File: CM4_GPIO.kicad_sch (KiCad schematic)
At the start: 0 parts

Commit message: Added footprints and symbols
Could not find -on SnapEDA- MCWR06X3322FTL, MCMR06X3162FTL and USB-A-S-VT.
Power load switch NCP380HSN05AAT1G only had footprint on SnapEDA, no symbol.
Need to update HMDI footprint and symbol to correct one.
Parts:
- added C? (x2): 100n, Capacitor_SMD:C_0402_1005Metric, symbol Device:C
- added J13: 1-2199119-5, 1-2199119-5:TE_1-2199119-5, symbol 1-2199119-5:1-2199119-5
- added J?: 690-019-298-412, CM4IO:EDAC 690-019-298-412, symbol CM4IO:HDMI_A_1.4
- added Module1: ComputeModule4, CM4IO:Raspberry-Pi-4-Compute-Module, symbol CM4IO:ComputeModule4-CM4
- added U?: RT9742SNGV, Package_TO_SOT_SMD:SOT-23, symbol CM4IO:RT9742SNGV
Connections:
- new net: J13.SH1 (SHIELD), J13.SH2 (SHIELD)
- new net +5v: C?.1, U?.1 (IN)
- new net CAM0_C_N: Module1.40 (GPIO9)
- new net CAM0_C_P: Module1.42 (GND)
- new net CAM0_D0_N: Module1.28 (GPIO13)
- new net CAM0_D0_P: Module1.30 (GPIO6)
- new net CAM0_D1_N: Module1.34 (GPIO5)
- new net CAM0_D1_P: Module1.36 (ID_SD)
- new net CAM1_C_N: Module1.27 (GPIO20)
- new net CAM1_C_P: Module1.29 (GPIO16)
- new net CAM1_D0_N: Module1.15 (Ethernet_nLED3(3.3v))
- new net CAM1_D0_P: Module1.17 (Ethernet_nLED2(3.3v))
- new net CAM1_D1_N: Module1.21 (PI_nLED_Activity)
- new net CAM1_D1_P: Module1.23 (GND)
- new net CAM1_D2_N: Module1.33 (GND)
- new net CAM1_D2_P: Module1.35 (ID_SC)
- new net CAM1_D3_N: Module1.39 (GPIO8)
- new net CAM1_D3_P: Module1.41 (GPIO25)
- new net DSI0_C_N: Module1.69 (SD_DAT2)
- new net DSI0_C_P: Module1.71 (GND)
- new net DSI0_D0_N: Module1.57 (SD_CLK)
- new net DSI0_D0_P: Module1.59 (GND)
- new net DSI0_D1_N: Module1.63 (SD_DAT0)
- new net DSI0_D1_P: Module1.65 (GND)
- new net DSI1_C_N: Module1.87 (+5v_(Input))
- new net DSI1_C_P: Module1.89 (WiFi_nDisable)
- new net DSI1_D0_N: Module1.75 (SD_PWR_ON)
- new net DSI1_D0_P: Module1.77 (+5v_(Input))
- new net DSI1_D1_N: Module1.81 (+5v_(Input))
- new net DSI1_D1_P: Module1.83 (+5v_(Input))
- new net DSI1_D2_N: Module1.93 (nRPIBOOT)
- new net DSI1_D2_P: Module1.95 (nPI_LED_PWR)
- new net DSI1_D3_N: Module1.94 (AnalogIP0)
- new net DSI1_D3_P: Module1.96 (AnalogIP1)
- new net GND: C?.2, C?.2, J?.11 (CKS), J?.17 (GND), J?.2 (D2S), J?.5 (D1S), J?.8 (D0S), J?.SH1 (SH), J?.SH2 (SH), J?.SH3 (SH), J?.SH4 (SH), Module1.13 (GND), Module1.14 (GND), Module1.19 (Ethernet_nLED1(3.3v)), Module1.20 (EEPROM_nWP), Module1.25 (GPIO21), Module1.26 (GPIO19), Module1.31 (GPIO12), Module1.32 (GND), Module1.37 (GPIO7), Module1.38 (GPIO11), Module1.44 (GPIO10), Module1.50 (GPIO17), Module1.55 (GPIO14), Module1.56 (GPIO3), Module1.61 (SD_DAT3), Module1.62 (SD_CMD), Module1.67 (SD_DAT1), Module1.68 (SD_DAT4), Module1.7 (GND), Module1.73 (SD_VDD_Override), Module1.74 (GND), Module1.79 (+5v_(Input)), Module1.8 (GND), Module1.80 (SCL0), Module1.85 (+5v_(Input)), Module1.86 (+3.3v_(Output)), Module1.91 (BT_nDisable), Module1.92 (RUN_PG), Module1.97 (Camera_GPIO), Module1.98 (GND), U?.3 (GND)
- new net HDMI0_CEC: J?.13 (CEC), Module1.51 (GPIO15)
- new net HDMI0_CK_N: J?.12 (CK-), Module1.90 (+1.8v_(Output))
- new net HDMI0_CK_P: J?.10 (CK+), Module1.88 (+1.8v_(Output))
- new net HDMI0_D0_N: J?.9 (D0-), Module1.84 (+3.3v_(Output))
- new net HDMI0_D0_P: J?.7 (D0+), Module1.82 (SDA0)
- new net HDMI0_D1_N: J?.6 (D1-), Module1.78 (GPIO_VREF(1.8v/3.3v_Input))
- new net HDMI0_D1_P: J?.4 (D1+), Module1.76 (Reserved)
- new net HDMI0_D2_N: J?.3 (D2-), Module1.72 (SD_DAT6)
- new net HDMI0_D2_P: J?.1 (D2+), Module1.70 (SD_DAT7)
- new net HDMI0_HOTPLUG: J?.19 (HPD/HEAC-), Module1.53 (GND)
- new net HDMI0_SCL: J?.15 (SCL), Module1.100 (nEXTRST)
- new net HDMI0_SDA: J?.16 (SDA), Module1.99 (Global_EN)
- new net HDMI1_CEC: Module1.49 (GPIO18)
- new net HDMI1_CK_N: Module1.66 (GND)
- new net HDMI1_CK_P: Module1.64 (SD_DAT5)
- new net HDMI1_D0_N: Module1.60 (GND)
- new net HDMI1_D0_P: Module1.58 (GPIO2)
- new net HDMI1_D1_N: Module1.54 (GPIO4)
- new net HDMI1_D1_P: Module1.52 (GND)
- new net HDMI1_D2_N: Module1.48 (GPIO27)
- new net HDMI1_D2_P: Module1.46 (GPIO22)
- new net HDMI1_HOTPLUG: Module1.43 (GND)
- new net HDMI1_SCL: Module1.47 (GPIO23)
- new net HDMI1_SDA: Module1.45 (GPIO24)
- new net HDMI_5v: C?.1, J?.18 (+5V), U?.2 (OUT)
- new net PCIE_CLK_N: Module1.12 (Ethernet_Pair0_P)
- new net PCIE_CLK_P: Module1.10 (Ethernet_Pair0_N)
- new net PCIE_CLK_nREQ: Module1.2 (GND)
- new net PCIE_RX_N: Module1.18 (Ethernet_SYNC_OUT(1.8v))
- new net PCIE_RX_P: Module1.16 (Ethernet_SYNC_IN(1.8v))
- new net PCIE_TX_N: Module1.24 (GPIO26)
- new net PCIE_TX_P: Module1.22 (GND)
- new net PCIE_nRST: Module1.9 (Ethernet_Pair2_N)
- new net TV_OUT: Module1.11 (Ethernet_Pair2_P)
- new net USB2_N: Module1.3 (Ethernet_Pair3_P)
- new net USB2_P: Module1.5 (Ethernet_Pair3_N)
- new net USBOTG_ID: Module1.1 (GND)
- no-connect marks 0 -> 3
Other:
- note added: "NVME Key-M"

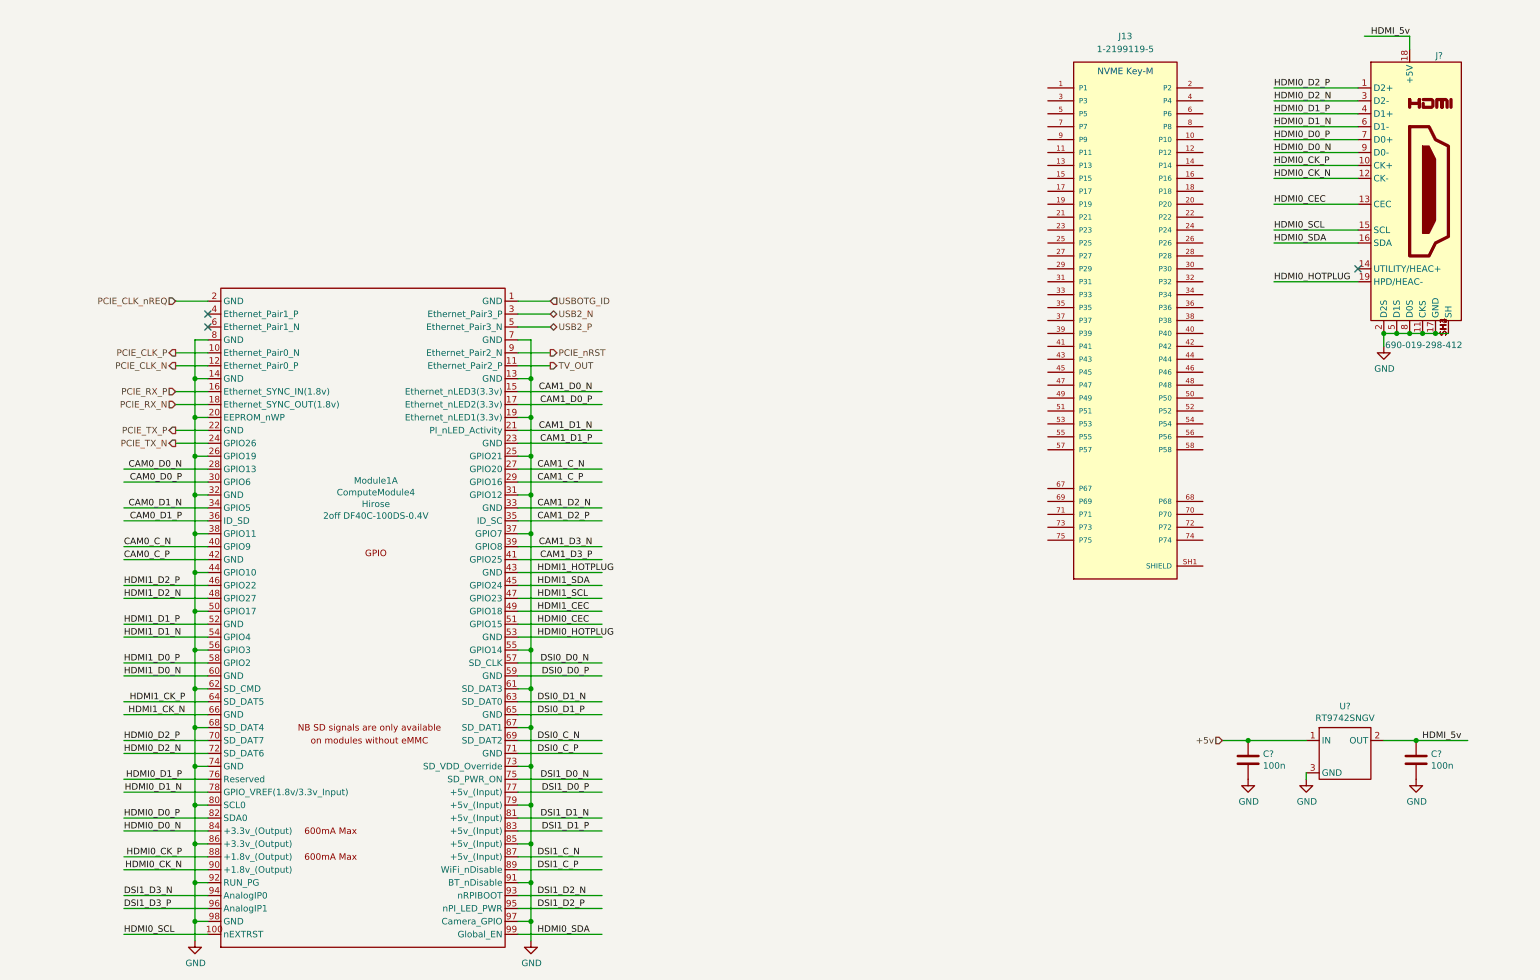
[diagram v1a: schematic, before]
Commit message: Added footprints for PCIe and added busses for PCIe and Ethernet
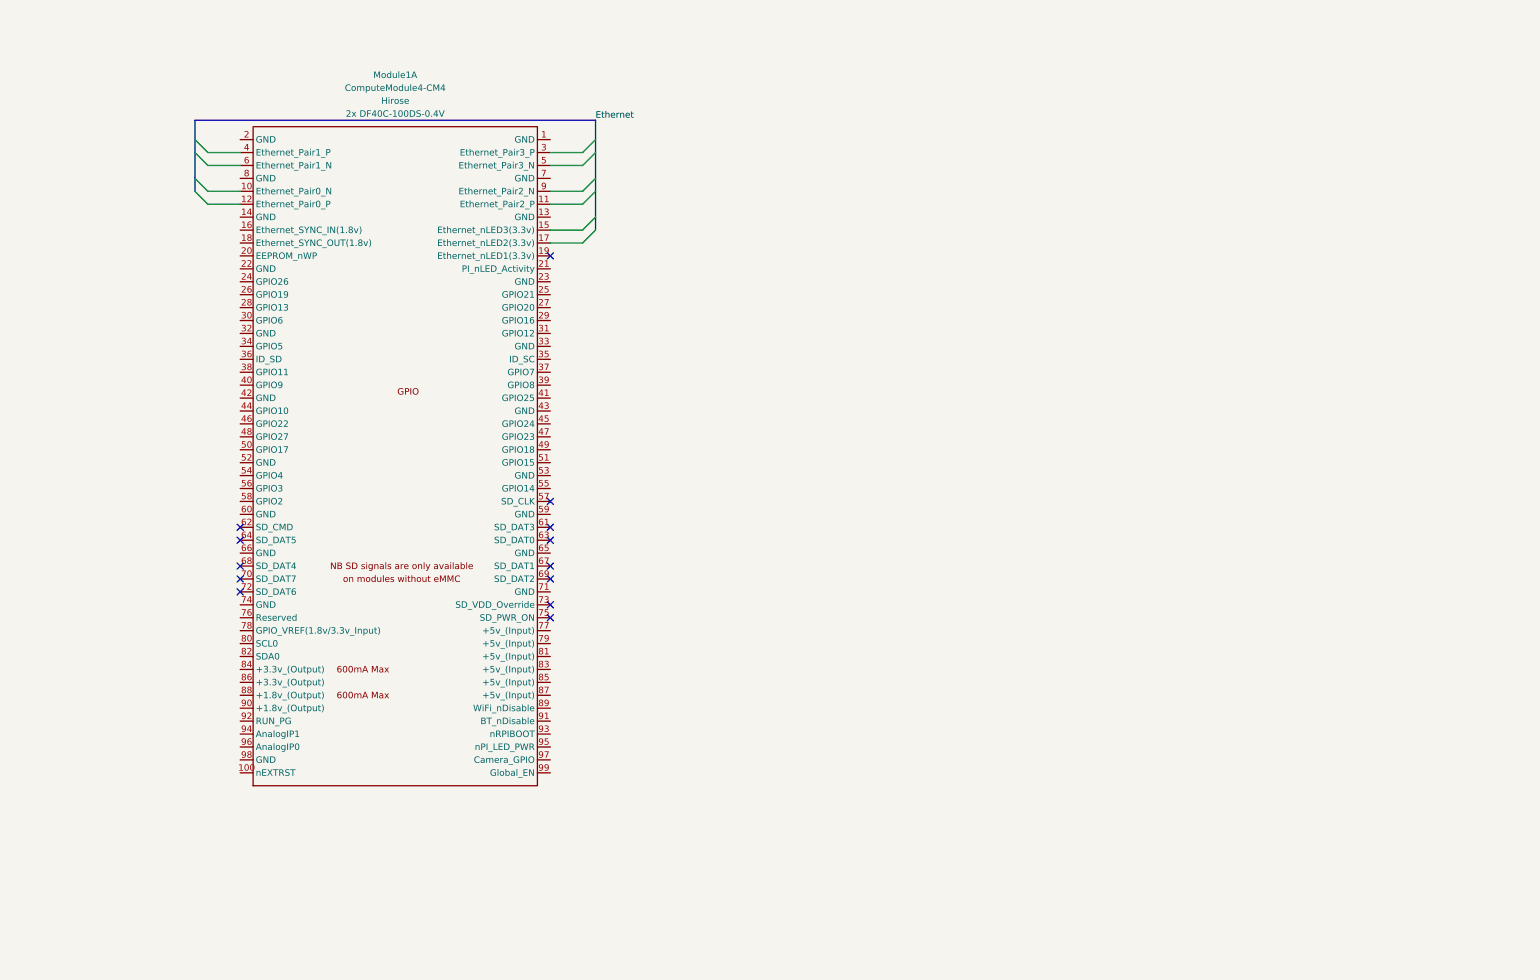
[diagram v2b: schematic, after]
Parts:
- removed C? (x2): 100n, Capacitor_SMD:C_0402_1005Metric, symbol Device:C
- removed J13: 1-2199119-5, 1-2199119-5:TE_1-2199119-5, symbol 1-2199119-5:1-2199119-5
- removed J?: 690-019-298-412, CM4IO:EDAC 690-019-298-412, symbol CM4IO:HDMI_A_1.4
- removed U?: RT9742SNGV, Package_TO_SOT_SMD:SOT-23, symbol CM4IO:RT9742SNGV
- Module1: value ComputeModule4 -> ComputeModule4-CM4; Field5 2off DF40C-100DS-0.4V -> 2x DF40C-100DS-0.4V; Field6 2off DF40C-100DS-0.4V -> (none); Field7 Hirose -> (none); Part Description 100 Position Connector Receptacle, Center Strip Contacts Su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 -> (none)
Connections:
- net CAM0_C_N: no longer names the net of Module1.40 (GPIO9)
- net CAM0_C_P: no longer names the net of Module1.42 (GND)
- net CAM0_D0_N: no longer names the net of Module1.28 (GPIO13)
- net CAM0_D0_P: no longer names the net of Module1.30 (GPIO6)
- net CAM0_D1_N: no longer names the net of Module1.34 (GPIO5)
- net CAM0_D1_P: no longer names the net of Module1.36 (ID_SD)
- net CAM1_C_N: no longer names the net of Module1.27 (GPIO20)
- net CAM1_C_P: no longer names the net of Module1.29 (GPIO16)
- net CAM1_D0_N: no longer names the net of Module1.15 (Ethernet_nLED3(3.3v))
- net CAM1_D0_P: no longer names the net of Module1.17 (Ethernet_nLED2(3.3v))
- net CAM1_D1_N: no longer names the net of Module1.21 (PI_nLED_Activity)
- net CAM1_D1_P: no longer names the net of Module1.23 (GND)
- net CAM1_D2_N: no longer names the net of Module1.33 (GND)
- net CAM1_D2_P: no longer names the net of Module1.35 (ID_SC)
- net CAM1_D3_N: no longer names the net of Module1.39 (GPIO8)
- net CAM1_D3_P: no longer names the net of Module1.41 (GPIO25)
- net DSI0_C_N: no longer names the net of Module1.69 (SD_DAT2)
- net DSI0_C_P: no longer names the net of Module1.71 (GND)
- net DSI0_D0_N: no longer names the net of Module1.57 (SD_CLK)
- net DSI0_D0_P: no longer names the net of Module1.59 (GND)
- net DSI0_D1_N: no longer names the net of Module1.63 (SD_DAT0)
- net DSI0_D1_P: no longer names the net of Module1.65 (GND)
- net DSI1_C_N: no longer names the net of Module1.87 (+5v_(Input))
- net DSI1_C_P: no longer names the net of Module1.89 (WiFi_nDisable)
- net DSI1_D0_N: no longer names the net of Module1.75 (SD_PWR_ON)
- net DSI1_D0_P: no longer names the net of Module1.77 (+5v_(Input))
- net DSI1_D1_N: no longer names the net of Module1.81 (+5v_(Input))
- net DSI1_D1_P: no longer names the net of Module1.83 (+5v_(Input))
- net DSI1_D2_N: no longer names the net of Module1.93 (nRPIBOOT)
- net DSI1_D2_P: no longer names the net of Module1.95 (nPI_LED_PWR)
- net DSI1_D3_N: no longer names the net of Module1.94 (AnalogIP1)
- net DSI1_D3_P: no longer names the net of Module1.96 (AnalogIP0)
- removed net GND: Module1.13 (GND), Module1.14 (GND), Module1.19 (Ethernet_nLED1(3.3v)), Module1.20 (EEPROM_nWP), Module1.25 (GPIO21), Module1.26 (GPIO19), Module1.31 (GPIO12), Module1.32 (GND), Module1.37 (GPIO7), Module1.38 (GPIO11), Module1.44 (GPIO10), Module1.50 (GPIO17), Module1.55 (GPIO14), Module1.56 (GPIO3), Module1.61 (SD_DAT3), Module1.62 (SD_CMD), Module1.67 (SD_DAT1), Module1.68 (SD_DAT4), Module1.7 (GND), Module1.73 (SD_VDD_Override), Module1.74 (GND), Module1.79 (+5v_(Input)), Module1.8 (GND), Module1.80 (SCL0), Module1.85 (+5v_(Input)), Module1.86 (+3.3v_(Output)), Module1.91 (BT_nDisable), Module1.92 (RUN_PG), Module1.97 (Camera_GPIO), Module1.98 (GND)
- net HDMI0_CEC: no longer names the net of Module1.51 (GPIO15)
- net HDMI0_CK_N: no longer names the net of Module1.90 (+1.8v_(Output))
- net HDMI0_CK_P: no longer names the net of Module1.88 (+1.8v_(Output))
- net HDMI0_D0_N: no longer names the net of Module1.84 (+3.3v_(Output))
- net HDMI0_D0_P: no longer names the net of Module1.82 (SDA0)
- net HDMI0_D1_N: no longer names the net of Module1.78 (GPIO_VREF(1.8v/3.3v_Input))
- net HDMI0_D1_P: no longer names the net of Module1.76 (Reserved)
- net HDMI0_D2_N: no longer names the net of Module1.72 (SD_DAT6)
- net HDMI0_D2_P: no longer names the net of Module1.70 (SD_DAT7)
- net HDMI0_HOTPLUG: no longer names the net of Module1.53 (GND)
- net HDMI0_SCL: no longer names the net of Module1.100 (nEXTRST)
- net HDMI0_SDA: no longer names the net of Module1.99 (Global_EN)
- net HDMI1_CEC: no longer names the net of Module1.49 (GPIO18)
- net HDMI1_CK_N: no longer names the net of Module1.66 (GND)
- net HDMI1_CK_P: no longer names the net of Module1.64 (SD_DAT5)
- net HDMI1_D0_N: no longer names the net of Module1.60 (GND)
- net HDMI1_D0_P: no longer names the net of Module1.58 (GPIO2)
- net HDMI1_D1_N: no longer names the net of Module1.54 (GPIO4)
- net HDMI1_D1_P: no longer names the net of Module1.52 (GND)
- net HDMI1_D2_N: no longer names the net of Module1.48 (GPIO27)
- net HDMI1_D2_P: no longer names the net of Module1.46 (GPIO22)
- net HDMI1_HOTPLUG: no longer names the net of Module1.43 (GND)
- net HDMI1_SCL: no longer names the net of Module1.47 (GPIO23)
- net HDMI1_SDA: no longer names the net of Module1.45 (GPIO24)
- net PCIE_CLK_N: no longer names the net of Module1.12 (Ethernet_Pair0_P)
- net PCIE_CLK_P: no longer names the net of Module1.10 (Ethernet_Pair0_N)
- net PCIE_CLK_nREQ: no longer names the net of Module1.2 (GND)
- net PCIE_RX_N: no longer names the net of Module1.18 (Ethernet_SYNC_OUT(1.8v))
- net PCIE_RX_P: no longer names the net of Module1.16 (Ethernet_SYNC_IN(1.8v))
- net PCIE_TX_N: no longer names the net of Module1.24 (GPIO26)
- net PCIE_TX_P: no longer names the net of Module1.22 (GND)
- net PCIE_nRST: no longer names the net of Module1.9 (Ethernet_Pair2_N)
- net TV_OUT: no longer names the net of Module1.11 (Ethernet_Pair2_P)
- net USB2_N: no longer names the net of Module1.3 (Ethernet_Pair3_P)
- net USB2_P: no longer names the net of Module1.5 (Ethernet_Pair3_N)
- net USBOTG_ID: no longer names the net of Module1.1 (GND)
- no-connect marks 3 -> 13
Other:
- note removed: "NVME Key-M"

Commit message: Cleaned up schematics and added gnds and no-connects
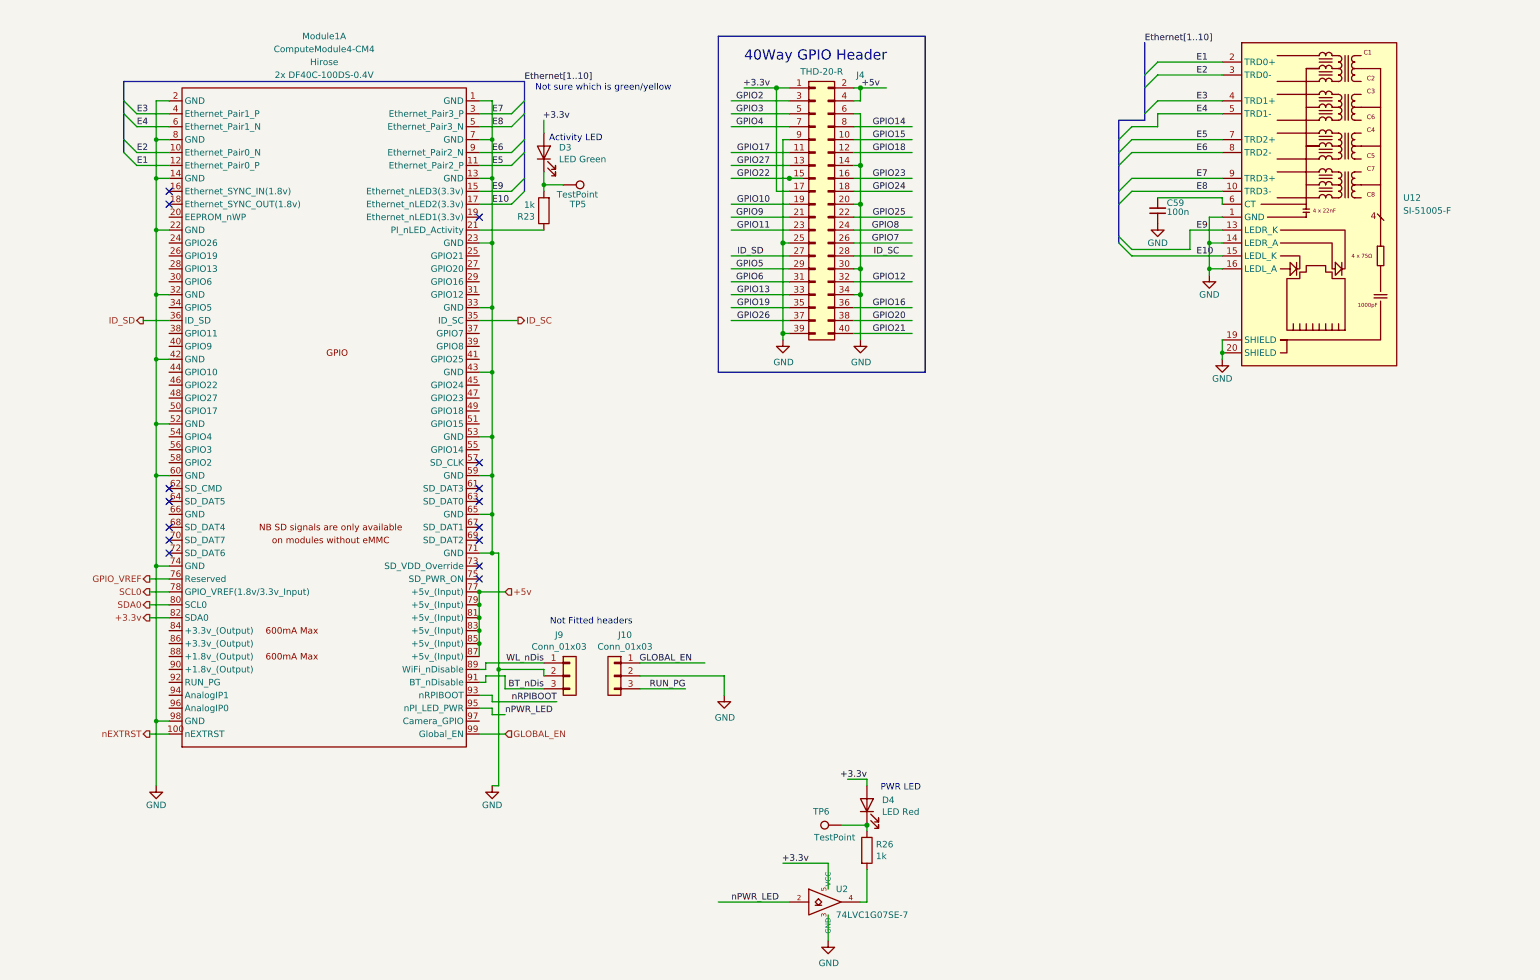
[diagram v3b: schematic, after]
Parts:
- added C59: 100n, symbol Device:C_Small
- added D3: LED Green, LED_SMD:LED_0603_1608Metric, symbol Device:LED
- added D4: LED Red, LED_SMD:LED_0603_1608Metric, symbol Device:LED
- added J10, J9: Conn_01x03, Connector_PinHeader_2.54mm:PinHeader_1x03_P2.54mm_Vertical, symbol Connector_Generic:Conn_01x03
- added J4: THD-20-R, Connector_PinHeader_2.54mm:PinHeader_2x20_P2.54mm_Vertical, symbol Connector_Generic:Conn_02x20_Odd_Even
- added R23, R26: 1k, Resistor_SMD:R_0402_1005Metric, symbol Device:R
- added TP5, TP6: TestPoint, TestPoint:TestPoint_Pad_2.0x2.0mm, symbol Connector:TestPoint
- added U12: SI-51005-F, Ethernet_con:TE_RJ45-8L-B, symbol SI-51005-F:SI-51005-F
- added U2: 74LVC1G07SE-7, Package_TO_SOT_SMD:SOT-353_SC-70-5, symbol CM4IO:74LVC1G07_copy
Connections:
- net GND: now reaches Module1.1 (GND)
- net GND: now also Module1.11 (Ethernet_Pair2_P), Module1.13 (GND), Module1.14 (GND), Module1.15 (Ethernet_nLED3(3.3v)), Module1.17 (Ethernet_nLED2(3.3v)), Module1.2 (GND), Module1.22 (GND), Module1.23 (GND), Module1.3 (Ethernet_Pair3_P), Module1.32 (GND), Module1.33 (GND), Module1.42 (GND), Module1.43 (GND), Module1.5 (Ethernet_Pair3_N), Module1.52 (GND), Module1.53 (GND), Module1.59 (GND), Module1.60 (GND), Module1.65 (GND), Module1.7 (GND), Module1.71 (GND), Module1.74 (GND), Module1.8 (GND), Module1.9 (Ethernet_Pair2_N), Module1.98 (GND), C59.1, J10.2 (Pin_2), J4.14 (Pin_14), J4.20 (Pin_20), J4.25 (Pin_25), J4.30 (Pin_30), J4.34 (Pin_34), J4.39 (Pin_39), J4.6 (Pin_6), J4.9 (Pin_9), J9.2 (Pin_2), U12.1 (GND), U12.10 (TRD3-), U12.13 (LEDR_K), U12.14 (LEDR_A), U12.15 (LEDL_K), U12.16 (LEDL_A), U12.19 (SHIELD), U12.20 (SHIELD), U12.7 (TRD2+), U12.8 (TRD2-), U12.9 (TRD3+), U2.3 (GND)
- net E2: now reaches Module1.10 (Ethernet_Pair0_N)
- net E2: now also U12.3 (TRD0-)
- net nEXTRST: now reaches Module1.100 (nEXTRST)
- net E1: now reaches Module1.12 (Ethernet_Pair0_P)
- net E1: now also U12.2 (TRD0+)
- net at Module1.21 (PI_nLED_Activity): now also R23.1
- net ID_SC: now reaches Module1.35 (ID_SC)
- net ID_SC: now also J4.28 (Pin_28)
- net ID_SD: now reaches Module1.36 (ID_SD)
- net ID_SD: now also J4.27 (Pin_27)
- net E3: now reaches Module1.4 (Ethernet_Pair1_P)
- net E3: now also U12.4 (TRD1+)
- net E4: now reaches Module1.6 (Ethernet_Pair1_N)
- net E4: now also U12.5 (TRD1-)
- net GPIO_VREF: now reaches Module1.76 (Reserved)
- net +5v: now reaches Module1.77 (+5v_(Input))
- net +5v: now also Module1.79 (+5v_(Input)), Module1.81 (+5v_(Input)), Module1.83 (+5v_(Input)), Module1.85 (+5v_(Input)), Module1.87 (+5v_(Input)), J4.2 (Pin_2), J4.4 (Pin_4)
- net SCL0: now reaches Module1.78 (GPIO_VREF(1.8v/3.3v_Input))
- net SDA0: now reaches Module1.80 (SCL0)
- net +3.3v: now reaches Module1.82 (SDA0)
- net +3.3v: now also D4.2 (A), J4.1 (Pin_1), J4.17 (Pin_17), U2.5 (VCC)
- net WL_nDis: now reaches Module1.89 (WiFi_nDisable)
- net WL_nDis: now also J9.1 (Pin_1)
- net BT_nDis: now reaches Module1.91 (BT_nDisable)
- net BT_nDis: now also J9.3 (Pin_3)
- net nRPIBOOT: now reaches Module1.93 (nRPIBOOT)
- net nPWR_LED: now reaches Module1.95 (nPI_LED_PWR)
- net nPWR_LED: now also U2.2
- net GLOBAL_EN: now reaches Module1.99 (Global_EN)
- net GLOBAL_EN: now also J10.1 (Pin_1)
- new net: D3.1 (K), R23.2, TP5.1
- new net: D4.1 (K), R26.1, TP6.1
- new net: R26.2, U2.4
- new net: C59.2, U12.6 (CT)
- new net GPIO10: J4.19 (Pin_19)
- new net GPIO11: J4.23 (Pin_23)
- new net GPIO12: J4.32 (Pin_32)
- new net GPIO13: J4.33 (Pin_33)
- new net GPIO14: J4.8 (Pin_8)
- new net GPIO15: J4.10 (Pin_10)
- new net GPIO16: J4.36 (Pin_36)
- new net GPIO17: J4.11 (Pin_11)
- new net GPIO18: J4.12 (Pin_12)
- new net GPIO19: J4.35 (Pin_35)
- new net GPIO2: J4.3 (Pin_3)
- new net GPIO20: J4.38 (Pin_38)
- new net GPIO21: J4.40 (Pin_40)
- new net GPIO22: J4.15 (Pin_15)
- new net GPIO23: J4.16 (Pin_16)
- new net GPIO24: J4.18 (Pin_18)
- new net GPIO25: J4.22 (Pin_22)
- new net GPIO26: J4.37 (Pin_37)
- new net GPIO27: J4.13 (Pin_13)
- new net GPIO3: J4.5 (Pin_5)
- new net GPIO4: J4.7 (Pin_7)
- new net GPIO5: J4.29 (Pin_29)
- new net GPIO6: J4.31 (Pin_31)
- new net GPIO7: J4.26 (Pin_26)
- new net GPIO8: J4.24 (Pin_24)
- new net GPIO9: J4.21 (Pin_21)
- new net RUN_PG: J10.3 (Pin_3)
- no-connect marks 13 -> 15
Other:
- note added: "40Way GPIO Header"
- note added: "Activity LED"
- note added: "Not Fitted headers"
- note added: "Not sure which is green/yellow"
- note added: "PWR LED"
- moved on the sheet: Module1A
